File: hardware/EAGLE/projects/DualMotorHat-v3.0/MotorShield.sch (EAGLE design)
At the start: 84 parts, among them IC0 TEENSY_3.1-3.2_ALL_PINS&PADS, IC2_0_PC JP, U0-C1 0.1uF, U0-C2 1nF, U0-C3 0.22uF, U0-C4 0.1uF, U0-C5 0.22uF, U0-R1 4.7k, U0-R2 47k, U0-R3 10k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

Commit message: Connector for Hat added
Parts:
- removed X2: RASPI_BOARD_B+_H, raspberrypi_bastelstube_v13:RASPI_BOARD_B+_H
- added J1, J2: (no value), SparkFun-Connectors:CONN_12NO_SILK
- added J3: (no value), SparkFun-Connectors:CONN_041X04_NO_SILK
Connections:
- removed net CS1: IC0.9/RX2/PWM, SPI_CONN0.1
- removed net CS2: IC0.15/A1/T, SPI_CONN1.1
- removed net MISO: IC0.12/MISO, SPI_CONN0.4, SPI_CONN1.4
- removed net MOSI: IC0.11/MOSI, SPI_CONN0.3, SPI_CONN1.3
- removed net SCK: IC0.13/SCK/LED, SPI_CONN0.2, SPI_CONN1.2
- removed net SCL0: IC0.19/A5/T/SCL0, IC2_0_PC.2
- removed net SCL1: I2C_1_IMU.2, IC0.29/A18/SCL1
- removed net SDA0: IC0.18/A4/T/SDA0, IC2_0_PC.1
- removed net SDA1: I2C_1_IMU.3, IC0.30/A19/SDA1
- new net I2C0_SCL: IC0.19/A5/T/SCL0, IC2_0_PC.2, X1.SCL
- new net I2C0_SDA: IC0.18/A4/T/SDA0, IC2_0_PC.1, X1.SDA
- new net I2C1_SCL: I2C_1_IMU.2, IC0.29/A18/SCL1, X1.ID_SC
- new net I2C1_SDA: I2C_1_IMU.3, IC0.30/A19/SDA1, X1.ID_SD
- new net N$4: J3.4
- new net N$5: J3.3
- new net N$6: J3.2
- new net N$7: J3.1
- new net SPI_CS0: IC0.9/RX2/PWM, SPI_CONN0.1, X1.SPI_CE0
- new net SPI_CS1: IC0.15/A1/T, SPI_CONN1.1, X1.SPI_CE1
- new net SPI_MISO: IC0.12/MISO, SPI_CONN0.4, SPI_CONN1.4, X1.SPI_MISO
- new net SPI_MOSI: IC0.11/MOSI, SPI_CONN0.3, SPI_CONN1.3, X1.SPI_MOSI
- new net SPI_SCLK: IC0.13/SCK/LED, SPI_CONN0.2, SPI_CONN1.2, X1.SPI_SCLK
- new net S_PWM_0: SERVO_0.2
- net HALL_U0: now also J1.1
- net HALL_V0: now also J1.2
- net HALL_W0: now also J1.3
- net INH_U0: now also J1.7
- net INH_V0: now also J1.8
- net INH_W0: now also J1.9
- net IN_U0: now also J1.4
- net IN_V0: now also J1.5
- net IN_W0: now also J1.6
- net IS_U0: now also J1.10
- net IS_V0: now also J1.11
- net IS_W0: now also J1.12
- net S_PWM_2: no longer SERVO_0.2

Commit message: layout update
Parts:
- removed IC0: TEENSY_3.1-3.2_ALL_PINS&PADS, Teensy_3_and_LC_Series_Boards_v1.4:TEENSY_3.1-3.2_ALL_PINS&PADS
- removed IN-PWM0, IN-PWM1: JP, SparkFun-Connectors:CONN_031X03_NO_SILK
- removed J3: (no value), SparkFun-Connectors:CONN_041X04_NO_SILK
- removed U$5: 5569-002, 5569-02:5569-002
- added BATTERY: (no value), SparkFun-Connectors:CONN_031X03_NO_SILK
- added SERVOS, VCC: (no value), SparkFun-Connectors:CONN_021X02_NO_SILK
- renumbered J1 to MOTOR_CONTRO_0, J2 to MOTOR_CONTROL_1
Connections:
- removed net HALL_U2: H1-R3.1, HALL1.2, IC0.14/A0
- removed net HALL_V2: H1-R2.1, HALL1.3, IC0.16/A2/T
- removed net HALL_W2: H1-R1.1, HALL1.4, IC0.17/A3/T
- removed net IN_U2_EX: IC0.21/A7/PWM
- removed net IN_U_EX: IC0.5/PWM
- removed net IN_V2_EX: IC0.22/A8/T/PWM
- removed net IN_V_EX: IC0.6/PWM
- removed net IN_W2_EX: IC0.23/A9/T/PWM
- removed net IN_W_EX: IC0.10/TX2/PWM
- removed net N$4: J3.4
- removed net N$5: J3.3
- removed net N$6: J3.2
- removed net N$7: J3.1
- removed net S_PWM_0: SERVO_0.2
- removed net S_PWM_1: IC0.32/T/PWM, SERVO_1.2
- removed net S_PWM_2: IC0.25/T/PWM
- new net HALL_U1: H1-R3.1, HALL1.2, MOTOR_CONTROL_1.1
- new net HALL_V1: H1-R2.1, HALL1.3, MOTOR_CONTROL_1.2
- new net HALL_W1: H1-R1.1, HALL1.4, MOTOR_CONTROL_1.3
- new net SERVO_0: SERVOS.1, SERVO_0.2
- new net SERVO_1: SERVOS.2, SERVO_1.2
- net 3.3V: no longer IC0.3.3V
- net GND: now also BATTERY.1, VCC.1; no longer IC0.GND, U$5.1
- net HALL_U0: no longer IC0.20/A6/PWM
- net HALL_V0: no longer IC0.A10
- net HALL_W0: no longer IC0.A11
- net I2C0_SCL: no longer IC0.19/A5/T/SCL0
- net I2C0_SDA: no longer IC0.18/A4/T/SDA0
- net I2C1_SCL: no longer IC0.29/A18/SCL1
- net I2C1_SDA: no longer IC0.30/A19/SDA1
- net INH_U0: no longer IC0.24
- net INH_U1: now also MOTOR_CONTROL_1.7; no longer IC0.2
- net INH_V0: no longer IC0.3/CAN-TX/PWM
- net INH_V1: now also MOTOR_CONTROL_1.8; no longer IC0.1/TX1/T
- net INH_W0: no longer IC0.33/T
- net INH_W1: now also MOTOR_CONTROL_1.9; no longer IC0.0/RX1/T
- net IN_U0: no longer IN-PWM0.3
- net IN_U1: now also MOTOR_CONTROL_1.4; no longer IN-PWM1.3
- net IN_V0: no longer IN-PWM0.2
- net IN_V1: now also MOTOR_CONTROL_1.5; no longer IN-PWM1.2
- net IN_W0: no longer IN-PWM0.1
- net IN_W1: now also MOTOR_CONTROL_1.6; no longer IN-PWM1.1
- net IS_U0: no longer IC0.26/A15
- net IS_U1: now also MOTOR_CONTROL_1.10; no longer IC0.31/A20
- net IS_V0: no longer IC0.27/A16
- net IS_V1: now also MOTOR_CONTROL_1.11; no longer IC0.A13
- net IS_W0: no longer IC0.28/A17
- net IS_W1: now also MOTOR_CONTROL_1.12; no longer IC0.A12
- net SPI_CS0: no longer IC0.9/RX2/PWM
- net SPI_CS1: no longer IC0.15/A1/T
- net SPI_MISO: no longer IC0.12/MISO
- net SPI_MOSI: no longer IC0.11/MOSI
- net SPI_SCLK: no longer IC0.13/SCK/LED
- net VCC: now also VCC.2; no longer IC0.VIN
- net VI: now also BATTERY.3; no longer U$5.2

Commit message: progress on MotorHat
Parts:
- removed MOTOR_CONTROL_1, MOTOR_CONTRO_0: (no value), SparkFun-Connectors:CONN_12NO_SILK
- added MOTOR0_CONTROL, MOTOR0_SENS, MOTOR1_CONTROL, MOTOR1_SENS: (no value), SparkFun-Connectors:CONN_06NO_SILK_NO_POP
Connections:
- net 3.3V: now also X1.3V3
- net HALL_U0: now also H0-R1.1, HALL0.4, MOTOR0_SENS.1; no longer H0-R3.1, HALL0.2, MOTOR_CONTRO_0.1
- net HALL_U1: now also H1-R1.1, HALL1.4, MOTOR1_SENS.1; no longer H1-R3.1, HALL1.2, MOTOR_CONTROL_1.1
- net HALL_V0: now also MOTOR0_SENS.2; no longer MOTOR_CONTRO_0.2
- net HALL_V1: now also MOTOR1_SENS.2; no longer MOTOR_CONTROL_1.2
- net HALL_W0: now also H0-R3.1, HALL0.2, MOTOR0_SENS.3; no longer H0-R1.1, HALL0.4, MOTOR_CONTRO_0.3
- net HALL_W1: now also H1-R3.1, HALL1.2, MOTOR1_SENS.3; no longer H1-R1.1, HALL1.4, MOTOR_CONTROL_1.3
- net INH_U0: now also MOTOR0_CONTROL.1; no longer MOTOR_CONTRO_0.7
- net INH_U1: now also MOTOR1_CONTROL.1; no longer MOTOR_CONTROL_1.7
- net INH_V0: now also MOTOR0_CONTROL.2; no longer MOTOR_CONTRO_0.8
- net INH_V1: now also MOTOR1_CONTROL.2; no longer MOTOR_CONTROL_1.8
- net INH_W0: now also MOTOR0_CONTROL.3; no longer MOTOR_CONTRO_0.9
- net INH_W1: now also MOTOR1_CONTROL.3; no longer MOTOR_CONTROL_1.9
- net IN_U0: now also MOTOR0_CONTROL.4; no longer MOTOR_CONTRO_0.4
- net IN_U1: now also MOTOR1_CONTROL.4; no longer MOTOR_CONTROL_1.4
- net IN_V0: now also MOTOR0_CONTROL.5; no longer MOTOR_CONTRO_0.5
- net IN_V1: now also MOTOR1_CONTROL.5; no longer MOTOR_CONTROL_1.5
- net IN_W0: now also MOTOR0_CONTROL.6; no longer MOTOR_CONTRO_0.6
- net IN_W1: now also MOTOR1_CONTROL.6; no longer MOTOR_CONTROL_1.6
- net IS_U0: now also MOTOR0_SENS.4; no longer MOTOR_CONTRO_0.10
- net IS_U1: now also MOTOR1_SENS.4; no longer MOTOR_CONTROL_1.10
- net IS_V0: now also MOTOR0_SENS.5; no longer MOTOR_CONTRO_0.11
- net IS_V1: now also MOTOR1_SENS.5; no longer MOTOR_CONTROL_1.11
- net IS_W0: now also MOTOR0_SENS.6; no longer MOTOR_CONTRO_0.12
- net IS_W1: now also MOTOR1_SENS.6; no longer MOTOR_CONTROL_1.12
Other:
- moved on the sheet: SERVOS, VCC

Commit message: update
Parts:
- removed VCC: (no value), SparkFun-Connectors:CONN_021X02_NO_SILK
- added J1: (no value), SparkFun-Connectors:CONN_031X03_NO_SILK
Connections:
- removed net VCC: SERVO_0.3, SERVO_1.3, U1.VO, VCC.2
- new net 5.0V: J1.2, SERVO_0.3, SERVO_1.3, U1.VO
- net 3.3V: now also J1.3; no longer X1.3V3
- net GND: now also J1.1; no longer VCC.1
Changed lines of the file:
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@@
 <part name="X1" library="raspberrypi_bastelstube_v13" deviceset="RASPI_BOARD_B+" device="_H"/>
 <part name="BATTERY" library="SparkFun-Connectors" deviceset="CONN_03" device="1X03_NO_SILK"/>
-<part name="VCC" library="SparkFun-Connectors" deviceset="CONN_02" device="1X02_NO_SILK"/>
 <part name="SERVOS" library="SparkFun-Connectors" deviceset="CONN_02" device="1X02_NO_SILK"/>
 <part name="MOTOR1_SENS" library="SparkFun-Connectors" deviceset="CONN_06" device="NO_SILK_NO_POP"/>
@@
 <part name="MOTOR0_CONTROL" library="SparkFun-Connectors" deviceset="CONN_06" device="NO_SILK_NO_POP"/>
 <part name="MOTOR1_CONTROL" library="SparkFun-Connectors" deviceset="CONN_06" device="NO_SILK_NO_POP"/>
+<part name="J1" library="SparkFun-Connectors" deviceset="CONN_03" device="1X03_NO_SILK"/>
 </parts>
 <sheets>
@@
 <attribute name="NAME" x="0" y="84.328" size="1.778" layer="95" font="vector"/>
 </instance>
-<instance part="VCC" gate="G$1" x="2.54" y="50.8" smashed="yes">
-<attribute name="VALUE" x="0" y="45.974" size="1.778" layer="96" font="vector"/>
-<attribute name="NAME" x="0" y="56.388" size="1.778" layer="95" font="vector"/>
-</instance>
 <instance part="SERVOS" gate="G$1" x="2.54" y="27.94" smashed="yes">
 <attribute name="VALUE" x="0" y="23.114" size="1.778" layer="96" font="vector"/>
@@
 <attribute name="VALUE" x="444.5" y="-108.966" size="1.778" layer="96" font="vector"/>
 <attribute name="NAME" x="444.5" y="-88.392" size="1.778" layer="95" font="vector"/>
+</instance>
+<instance part="J1" gate="J$1" x="2.54" y="53.34" smashed="yes">
+<attribute name="VALUE" x="0" y="45.974" size="1.778" layer="96" font="vector"/>
+<attribute name="NAME" x="0" y="58.928" size="1.778" layer="95" font="vector"/>
 </instance>
 </instances>
@@
 <wire x1="10.16" y1="50.8" x2="12.7" y2="50.8" width="0.1524" layer="91"/>
 <label x="12.7" y="50.8" size="1.778" layer="95" xref="yes"/>
-<pinref part="VCC" gate="G$1" pin="1"/>
+<pinref part="J1" gate="J$1" pin="1"/>
 </segment>
 </net>
@@
 </segment>
 </net>
-<net name="VCC" class="0">
+<net name="5.0V" class="0">
 <segment>
 <pinref part="SERVO_0" gate="J$1" pin="3"/>
@@
 <wire x1="10.16" y1="53.34" x2="20.32" y2="53.34" width="0.1524" layer="91"/>
 <label x="20.32" y="53.34" size="1.778" layer="95" xref="yes"/>
-<pinref part="VCC" gate="G$1" pin="2"/>
+<pinref part="J1" gate="J$1" pin="2"/>
 </segment>
 </net>
@@
 </segment>
 <segment>
-<pinref part="X1" gate="G$1" pin="3V3"/>
-<wire x1="162.56" y1="-50.8" x2="162.56" y2="-40.64" width="0.1524" layer="91"/>
-<wire x1="162.56" y1="-40.64" x2="175.26" y2="-40.64" width="0.1524" layer="91"/>
-<label x="175.26" y="-40.64" size="1.778" layer="95" xref="yes"/>
-</segment>
-</net>
+<pinref part="J1" gate="J$1" pin="3"/>
+<wire x1="10.16" y1="55.88" x2="12.7" y2="55.88" width="0.1524" layer="91"/>
+<label x="12.7" y="55.88" size="1.778" layer="95" xref="yes"/>
+</segment>
+</net>

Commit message: update
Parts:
- renumbered J1 to VCC
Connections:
- net N$1 renamed HB_INH_W0
- net N$10 renamed SR_U0
- net N$11 renamed HB_INH_U0
- net N$14 renamed HB_IN_U0
- net N$17 renamed HB_INH_U1
- net N$18 renamed HB_INH_V0
- net N$19 renamed HB_IN_U1
- net N$2 renamed SR_V0
- net N$20 renamed HB_IN_W0
- net N$23 renamed SR_U1
- net N$24 renamed HB_IN_V0
- net N$26 renamed HB_INH_V1
- net N$27 renamed HB_IN_V1
- net N$29 renamed SR_V1
- net N$3 renamed SR_W0
- net N$30 renamed HB_INH_W1
- net N$31 renamed HB_IN_W1
- net N$33 renamed SR_W1
- net GND: now also U0-C1.1, U0-C4.1, U1-C1.1, U1-C4.1, V0-C1.1, V0-C4.1, V1-C1.1, V1-C4.1, W0-C1.1, W0-C4.1, W1-C1.1, W1-C4.1; no longer U0-C1.2, U0-C4.2, U1-C1.2, U1-C4.2, V0-C1.2, V0-C4.2, V1-C1.2, V1-C4.2, W0-C1.2, W0-C4.2, W1-C1.2, W1-C4.2
- net IS_U0: now also U0-C1.2; no longer U0-C1.1
- net IS_U1: now also U1-C1.2; no longer U1-C1.1
- net IS_V0: now also V0-C1.2; no longer V0-C1.1
- net IS_V1: now also V1-C1.2; no longer V1-C1.1
- net IS_W0: now also W0-C1.2; no longer W0-C1.1
- net IS_W1: now also W1-C1.2; no longer W1-C1.1
- net VI: now also U0-C4.2, U1-C4.2, V0-C4.2, V1-C4.2, W0-C4.2, W1-C4.2; no longer U0-C4.1, U1-C4.1, V0-C4.1, V1-C4.1, W0-C4.1, W1-C4.1
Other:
- moved on the sheet: U0-C1, U0-C4, U1-C1, U1-C4, V0-C1, V0-C4, V1-C1, V1-C4, W0-C1, W0-C4, W1-C1, W1-C4

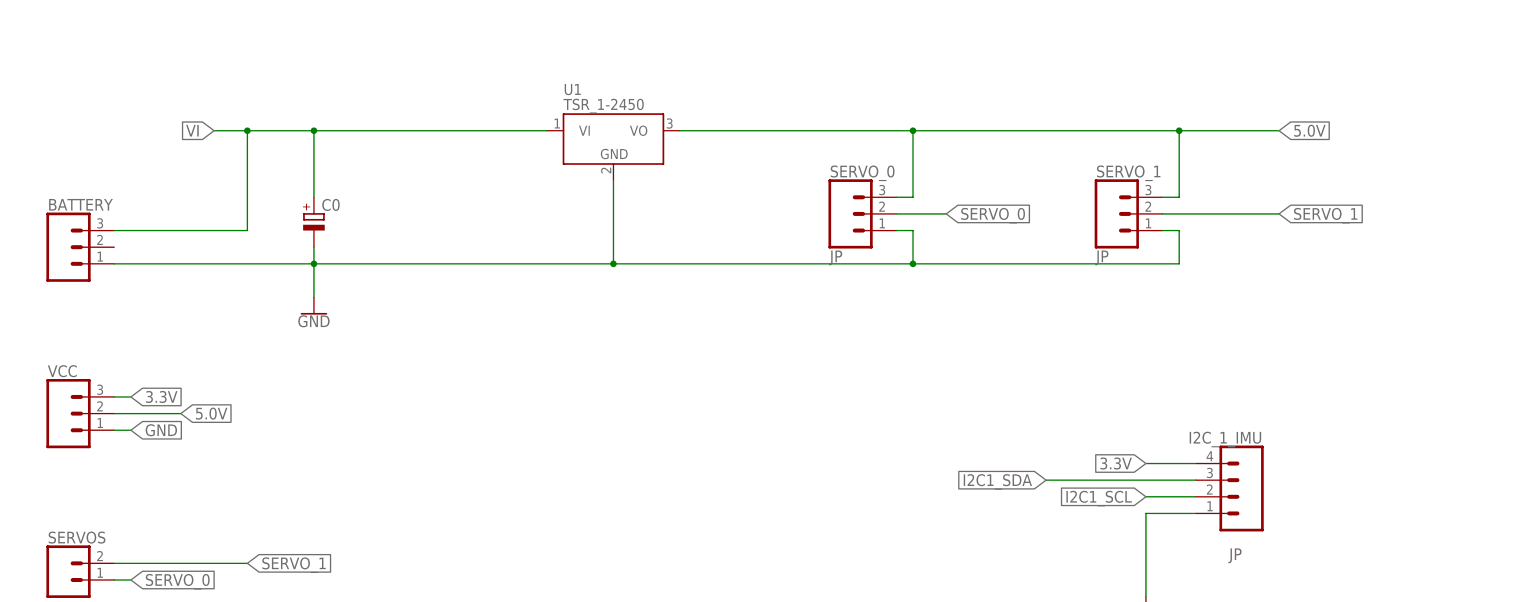
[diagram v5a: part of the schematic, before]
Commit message: vcc jumper update
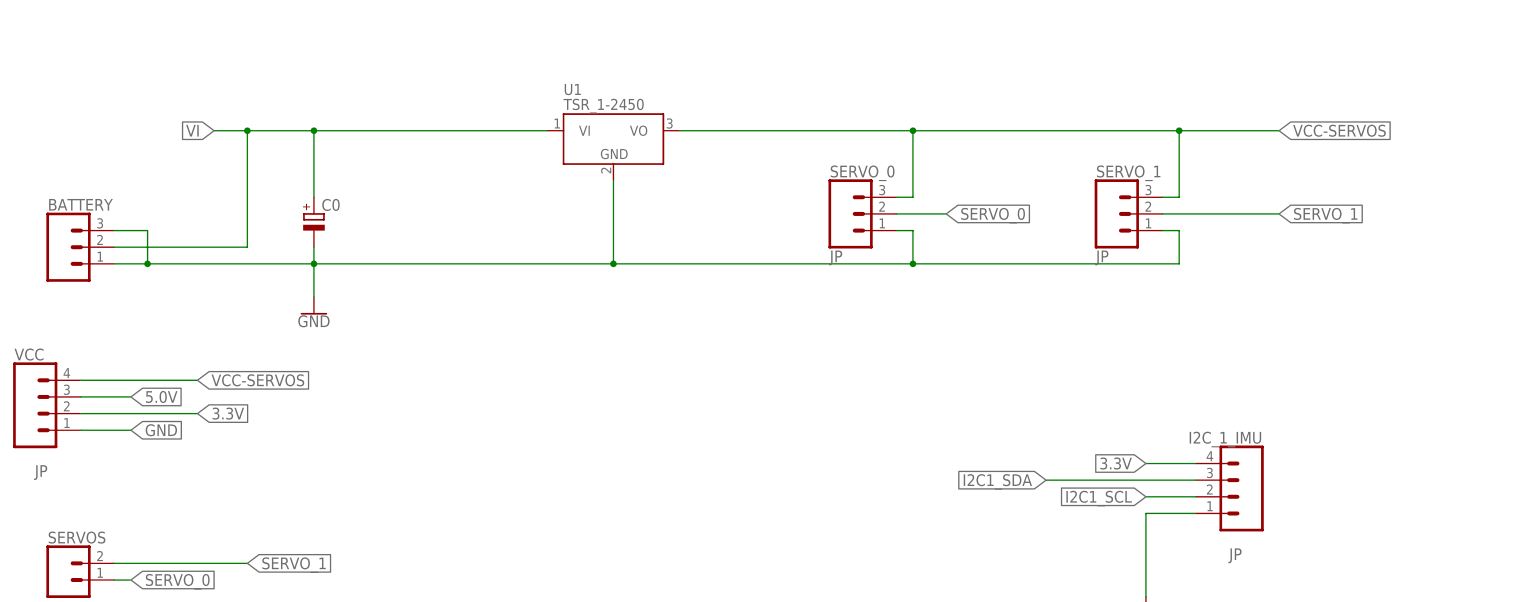
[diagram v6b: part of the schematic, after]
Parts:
- VCC: value (none) -> JP; device SparkFun-Connectors:CONN_031X03_NO_SILK -> SparkFun-Connectors:CONN_041X04_NO_SILK
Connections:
- new net VCC-SERVOS: SERVO_0.3, SERVO_1.3, U1.VO, VCC.4
- net 3.3V: now also VCC.2; no longer VCC.3
- net 5.0V: now also VCC.3; no longer SERVO_0.3, SERVO_1.3, U1.VO, VCC.2
- net GND: now also BATTERY.3
- net VI: now also BATTERY.2; no longer BATTERY.3
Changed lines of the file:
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@@
 <setting verticaltext="up"/>
 </settings>
-<grid distance="0.1" unitdist="inch" unit="inch" style="lines" multiple="5" display="yes" altdistance="0.01" altunitdist="inch" altunit="inch"/>
+<grid distance="0.1" unitdist="inch" unit="inch" style="lines" multiple="1" display="no" altdistance="0.01" altunitdist="inch" altunit="inch"/>
 <layers>
 <layer number="1" name="Top" color="4" fill="1" visible="no" active="no"/>
@@
 <part name="MOTOR0_CONTROL" library="SparkFun-Connectors" deviceset="CONN_06" device="NO_SILK_NO_POP"/>
 <part name="MOTOR1_CONTROL" library="SparkFun-Connectors" deviceset="CONN_06" device="NO_SILK_NO_POP"/>
-<part name="VCC" library="SparkFun-Connectors" deviceset="CONN_03" device="1X03_NO_SILK"/>
+<part name="VCC" library="SparkFun-Connectors" deviceset="CONN_04" device="1X04_NO_SILK" value="JP"/>
 </parts>
 <sheets>
@@
 <attribute name="NAME" x="444.5" y="-88.392" size="1.778" layer="95" font="vector"/>
 </instance>
-<instance part="VCC" gate="J$1" x="2.54" y="53.34" smashed="yes">
-<attribute name="VALUE" x="0" y="45.974" size="1.778" layer="96" font="vector"/>
-<attribute name="NAME" x="0" y="58.928" size="1.778" layer="95" font="vector"/>
+<instance part="VCC" gate="G$1" x="0" y="53.34" smashed="yes">
+<attribute name="VALUE" x="0" y="45.466" size="1.778" layer="96" font="vector" rot="R180"/>
+<attribute name="NAME" x="-5.08" y="61.468" size="1.778" layer="95" font="vector"/>
 </instance>
 </instances>
@@
 <pinref part="C0" gate="G$1" pin="-"/>
 <wire x1="40.64" y1="76.2" x2="40.64" y2="78.74" width="0.1524" layer="91"/>
-<wire x1="10.16" y1="76.2" x2="40.64" y2="76.2" width="0.1524" layer="91"/>
+<wire x1="10.16" y1="76.2" x2="15.24" y2="76.2" width="0.1524" layer="91"/>
 <junction x="40.64" y="76.2"/>
+<wire x1="15.24" y1="76.2" x2="40.64" y2="76.2" width="0.1524" layer="91"/>
 <wire x1="40.64" y1="76.2" x2="40.64" y2="71.12" width="0.1524" layer="91"/>
 <pinref part="U1" gate="G$1" pin="GND"/>
@@
 <wire x1="172.72" y1="76.2" x2="132.08" y2="76.2" width="0.1524" layer="91"/>
 <pinref part="BATTERY" gate="J$1" pin="1"/>
+<pinref part="BATTERY" gate="J$1" pin="3"/>
+<wire x1="10.16" y1="81.28" x2="15.24" y2="81.28" width="0.1524" layer="91"/>
+<wire x1="15.24" y1="81.28" x2="15.24" y2="76.2" width="0.1524" layer="91"/>
+<junction x="15.24" y="76.2"/>
 </segment>
 <segment>
@@
 </segment>
 <segment>
-<wire x1="10.16" y1="50.8" x2="12.7" y2="50.8" width="0.1524" layer="91"/>
+<wire x1="5.08" y1="50.8" x2="12.7" y2="50.8" width="0.1524" layer="91"/>
 <label x="12.7" y="50.8" size="1.778" layer="95" xref="yes"/>
-<pinref part="VCC" gate="J$1" pin="1"/>
+<pinref part="VCC" gate="G$1" pin="1"/>
 </segment>
 </net>
@@
 </segment>
 </net>
-<net name="5.0V" class="0">
+<net name="VCC-SERVOS" class="0">
 <segment>
 <pinref part="SERVO_0" gate="J$1" pin="3"/>
@@
 </segment>
 <segment>
-<wire x1="10.16" y1="53.34" x2="20.32" y2="53.34" width="0.1524" layer="91"/>
-<label x="20.32" y="53.34" size="1.778" layer="95" xref="yes"/>
-<pinref part="VCC" gate="J$1" pin="2"/>
+<pinref part="VCC" gate="G$1" pin="4"/>
+<wire x1="5.08" y1="58.42" x2="22.86" y2="58.42" width="0.1524" layer="91"/>
+<label x="22.86" y="58.42" size="1.778" layer="95" xref="yes"/>
 </segment>
 </net>
@@
 <wire x1="30.48" y1="96.52" x2="25.4" y2="96.52" width="0.1524" layer="91"/>
 <pinref part="C0" gate="G$1" pin="+"/>
-<wire x1="30.48" y1="96.52" x2="30.48" y2="81.28" width="0.1524" layer="91"/>
+<wire x1="30.48" y1="96.52" x2="30.48" y2="78.74" width="0.1524" layer="91"/>
 <junction x="30.48" y="96.52"/>
 <wire x1="40.64" y1="86.36" x2="40.64" y2="96.52" width="0.1524" layer="91"/>
 <junction x="40.64" y="96.52"/>
-<pinref part="BATTERY" gate="J$1" pin="3"/>
-<wire x1="10.16" y1="81.28" x2="30.48" y2="81.28" width="0.1524" layer="91"/>
+<pinref part="BATTERY" gate="J$1" pin="2"/>
+<wire x1="10.16" y1="78.74" x2="30.48" y2="78.74" width="0.1524" layer="91"/>
 </segment>
 <segment>
@@
 </segment>
 <segment>
-<pinref part="VCC" gate="J$1" pin="3"/>
-<wire x1="10.16" y1="55.88" x2="12.7" y2="55.88" width="0.1524" layer="91"/>
-<label x="12.7" y="55.88" size="1.778" layer="95" xref="yes"/>
+<wire x1="5.08" y1="53.34" x2="22.86" y2="53.34" width="0.1524" layer="91"/>
+<label x="22.86" y="53.34" size="1.778" layer="95" xref="yes"/>
+<pinref part="VCC" gate="G$1" pin="2"/>
 </segment>
 </net>
@@
 </segment>
 </net>
+<net name="5.0V" class="0">
+<segment>
+<pinref part="VCC" gate="G$1" pin="3"/>
+<wire x1="5.08" y1="55.88" x2="12.7" y2="55.88" width="0.1524" layer="91"/>
+<label x="12.7" y="55.88" size="1.778" layer="95" xref="yes"/>
+</segment>
+</net>
